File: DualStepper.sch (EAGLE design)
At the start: 12 parts

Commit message: Changed wire connectors to 5 mm grid
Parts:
- X1, X2: device con-phoenix-254:MPT4 -> con-ptr500:AK500/4
- X3: device con-phoenix-254:MPT2 -> con-ptr500:AK500/2
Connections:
- net +24V: now also X3-1.KL; no longer X3-2.1
- net GND: now also X3-2.KL; no longer X3-1.1
- net N$1: now also X1-1.KL; no longer X1-4.1
- net N$2: now also X1-2.KL; no longer X1-3.1
- net N$3: now also X1-3.KL; no longer X1-2.1
- net N$4: now also X1-4.KL; no longer X1-1.1
- net N$5: now also X2-4.KL; no longer X2-1.1
- net N$6: now also X2-3.KL; no longer X2-2.1
- net N$7: now also X2-2.KL; no longer X2-3.1
- net N$8: now also X2-1.KL; no longer X2-4.1
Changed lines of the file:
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@@
 <classes>
 <class number="0" name="default" width="0" drill="0">
-<clearance class="0" value="0.205"/>
 </class>
 </classes>
@@
 <part name="B1" library="we-board" deviceset="STEPSTICK" device="-TP"/>
 <part name="B2" library="we-board" deviceset="STEPSTICK" device="-TP"/>
-<part name="X1" library="con-phoenix-254" deviceset="MPT4" device=""/>
 <part name="GND1" library="supply1" deviceset="GND" device=""/>
 <part name="GND2" library="supply1" deviceset="GND" device=""/>
@@
 </part>
 <part name="GND4" library="supply1" deviceset="GND" device=""/>
-<part name="X3" library="con-phoenix-254" deviceset="MPT2" device=""/>
 <part name="GND5" library="supply1" deviceset="GND" device=""/>
 <part name="P+7" library="supply1" deviceset="+5V" device=""/>
@@
 <part name="GND7" library="supply1" deviceset="GND" device=""/>
 <part name="GND8" library="supply1" deviceset="GND" device=""/>
-<part name="X2" library="con-phoenix-254" deviceset="MPT4" device=""/>
+<part name="X1" library="con-ptr500" deviceset="AK500/4" device=""/>
+<part name="X2" library="con-ptr500" deviceset="AK500/4" device=""/>
+<part name="X3" library="con-ptr500" deviceset="AK500/2" device=""/>
 </parts>
 <sheets>
@@
 <instance part="B1" gate="BOARD" x="68.58" y="58.42"/>
 <instance part="B2" gate="BOARD" x="68.58" y="12.7"/>
-<instance part="X1" gate="-1" x="114.3" y="73.66"/>
-<instance part="X1" gate="-2" x="114.3" y="68.58"/>
-<instance part="X1" gate="-3" x="114.3" y="63.5"/>
-<instance part="X1" gate="-4" x="114.3" y="58.42"/>
 <instance part="GND1" gate="1" x="83.82" y="40.64"/>
 <instance part="GND2" gate="1" x="83.82" y="-7.62"/>
@@
 </instance>
 <instance part="GND4" gate="1" x="2.54" y="38.1"/>
-<instance part="X3" gate="-1" x="-15.24" y="71.12" rot="R180"/>
-<instance part="X3" gate="-2" x="-15.24" y="76.2" rot="R180"/>
 <instance part="GND5" gate="1" x="-7.62" y="71.12" rot="R90"/>
 <instance part="P+7" gate="1" x="17.78" y="30.48" rot="R180"/>
@@
 <instance part="GND7" gate="1" x="50.8" y="73.66" rot="R270"/>
 <instance part="GND8" gate="1" x="50.8" y="27.94" rot="R270"/>
-<instance part="X2" gate="-1" x="114.3" y="27.94"/>
-<instance part="X2" gate="-2" x="114.3" y="22.86"/>
-<instance part="X2" gate="-3" x="114.3" y="17.78"/>
-<instance part="X2" gate="-4" x="114.3" y="12.7"/>
+<instance part="X1" gate="-1" x="116.84" y="58.42" rot="R180"/>
+<instance part="X1" gate="-2" x="116.84" y="63.5" rot="R180"/>
+<instance part="X1" gate="-3" x="116.84" y="68.58" rot="R180"/>
+<instance part="X1" gate="-4" x="116.84" y="73.66" rot="R180"/>
+<instance part="X2" gate="-1" x="116.84" y="12.7" rot="R180"/>
+<instance part="X2" gate="-2" x="116.84" y="17.78" rot="R180"/>
+<instance part="X2" gate="-3" x="116.84" y="22.86" rot="R180"/>
+<instance part="X2" gate="-4" x="116.84" y="27.94" rot="R180"/>
+<instance part="X3" gate="-1" x="-17.78" y="76.2"/>
+<instance part="X3" gate="-2" x="-17.78" y="71.12"/>
 </instances>
 <busses>
@@
 </segment>
 <segment>
-<pinref part="X3" gate="-1" pin="1"/>
 <pinref part="GND5" gate="1" pin="GND"/>
 <wire x1="-12.7" y1="71.12" x2="-10.16" y2="71.12" width="0.1524" layer="91"/>
+<pinref part="X3" gate="-2" pin="KL"/>
 </segment>
 <segment>
@@
 <net name="+24V" class="0">
 <segment>
-<pinref part="X3" gate="-2" pin="1"/>
 <pinref part="P+6" gate="1" pin="+24V"/>
 <wire x1="-12.7" y1="76.2" x2="-10.16" y2="76.2" width="0.1524" layer="91"/>
+<pinref part="X3" gate="-1" pin="KL"/>
 </segment>
 <segment>
@@
 <net name="N$1" class="0">
 <segment>
-<pinref part="X1" gate="-4" pin="1"/>
 <pinref part="B1" gate="BOARD" pin="M2B"/>
 <wire x1="111.76" y1="58.42" x2="81.28" y2="58.42" width="0.1524" layer="91"/>
+<pinref part="X1" gate="-1" pin="KL"/>
 </segment>
 </net>
 <net name="N$2" class="0">
 <segment>
-<pinref part="X1" gate="-3" pin="1"/>
 <pinref part="B1" gate="BOARD" pin="M2A"/>
 <wire x1="111.76" y1="63.5" x2="81.28" y2="63.5" width="0.1524" layer="91"/>
+<pinref part="X1" gate="-2" pin="KL"/>
 </segment>
 </net>
 <net name="N$3" class="0">
 <segment>
-<pinref part="X1" gate="-2" pin="1"/>
 <pinref part="B1" gate="BOARD" pin="M1A"/>
 <wire x1="111.76" y1="68.58" x2="81.28" y2="68.58" width="0.1524" layer="91"/>
+<pinref part="X1" gate="-3" pin="KL"/>
 </segment>
 </net>
 <net name="N$4" class="0">
 <segment>
-<pinref part="X1" gate="-1" pin="1"/>
 <pinref part="B1" gate="BOARD" pin="M1B"/>
 <wire x1="111.76" y1="73.66" x2="81.28" y2="73.66" width="0.1524" layer="91"/>
+<pinref part="X1" gate="-4" pin="KL"/>
 </segment>
 </net>
@@
 <segment>
 <pinref part="B2" gate="BOARD" pin="M1B"/>
-<pinref part="X2" gate="-1" pin="1"/>
 <wire x1="81.28" y1="27.94" x2="111.76" y2="27.94" width="0.1524" layer="91"/>
+<pinref part="X2" gate="-4" pin="KL"/>
 </segment>
 </net>
@@
 <segment>
 <pinref part="B2" gate="BOARD" pin="M1A"/>
-<pinref part="X2" gate="-2" pin="1"/>
 <wire x1="81.28" y1="22.86" x2="111.76" y2="22.86" width="0.1524" layer="91"/>
+<pinref part="X2" gate="-3" pin="KL"/>
 </segment>
 </net>
@@
 <segment>
 <pinref part="B2" gate="BOARD" pin="M2A"/>
-<pinref part="X2" gate="-3" pin="1"/>
 <wire x1="81.28" y1="17.78" x2="111.76" y2="17.78" width="0.1524" layer="91"/>
+<pinref part="X2" gate="-2" pin="KL"/>
 </segment>
 </net>
@@
 <segment>
 <pinref part="B2" gate="BOARD" pin="M2B"/>
-<pinref part="X2" gate="-4" pin="1"/>
 <wire x1="81.28" y1="12.7" x2="111.76" y2="12.7" width="0.1524" layer="91"/>
-</segment>
-</net>
+<pinref part="X2" gate="-1" pin="KL"/>
+</segment>
+</net>

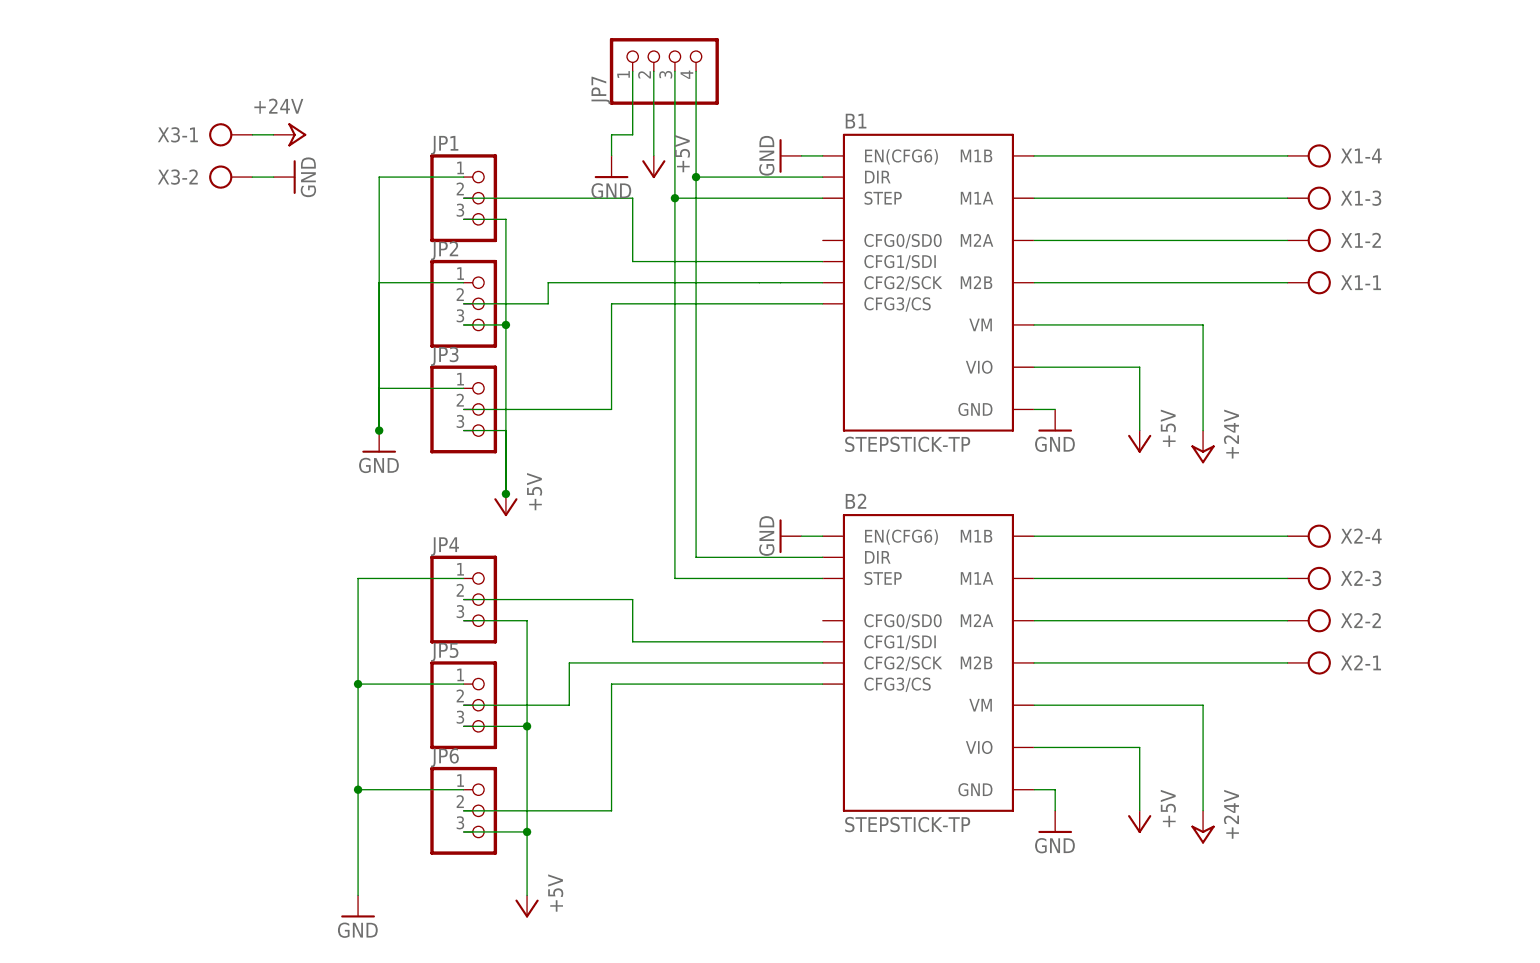
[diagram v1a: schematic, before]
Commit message: Changed connectors to 3.5 RT
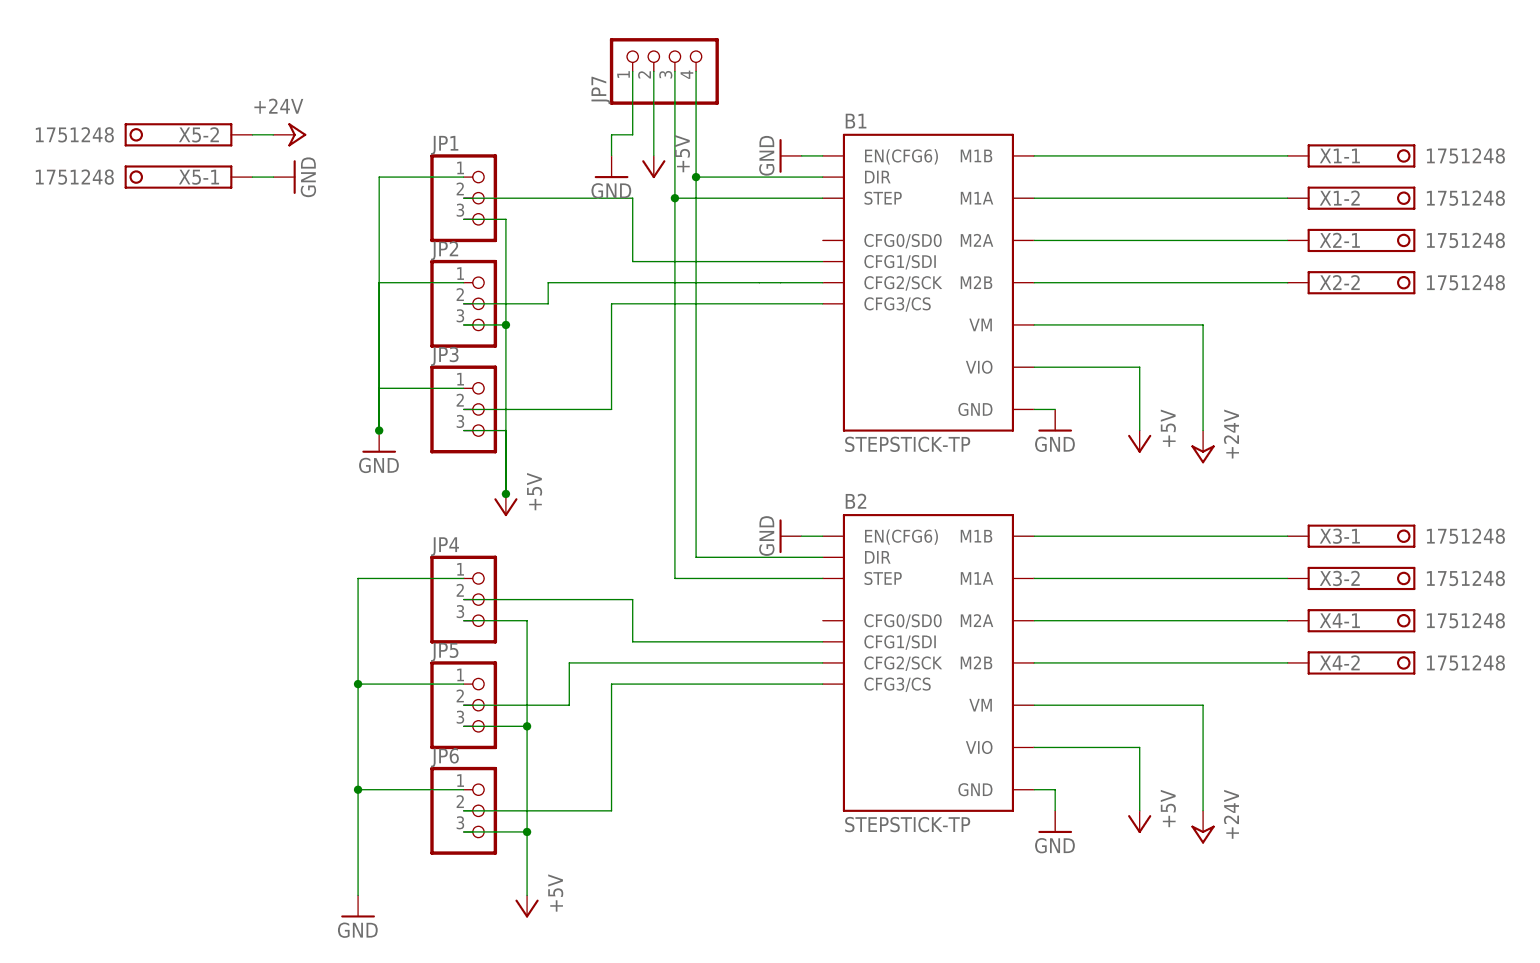
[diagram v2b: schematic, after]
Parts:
- added X4, X5: 1751248, con-phoenix-350:1751248
- X1, X2: value (none) -> 1751248; device con-ptr500:AK500/4 -> con-phoenix-350:1751248
- X3: value (none) -> 1751248; device con-ptr500:AK500/2 -> con-phoenix-350:1751248
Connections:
- net +24V: now also X5-2.K; no longer X3-1.KL
- net GND: now also X5-1.K; no longer X3-2.KL
- net N$1: now also X2-2.K; no longer X1-1.KL
- net N$2: now also X2-1.K; no longer X1-2.KL
- net N$3: now also X1-2.K; no longer X1-3.KL
- net N$4: now also X1-1.K; no longer X1-4.KL
- net N$5: now also X3-1.K; no longer X2-4.KL
- net N$6: now also X3-2.K; no longer X2-3.KL
- net N$7: now also X4-1.K; no longer X2-2.KL
- net N$8: now also X4-2.K; no longer X2-1.KL
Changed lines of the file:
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@@
 <grid distance="0.1" unitdist="inch" unit="inch" style="lines" multiple="1" display="no" altdistance="0.01" altunitdist="inch" altunit="inch"/>
 <layers>
-<layer number="1" name="Top" color="4" fill="1" visible="no" active="no"/>
-<layer number="16" name="Bottom" color="1" fill="1" visible="no" active="no"/>
-<layer number="17" name="Pads" color="2" fill="1" visible="no" active="no"/>
-<layer number="18" name="Vias" color="2" fill="1" visible="no" active="no"/>
-<layer number="19" name="Unrouted" color="6" fill="1" visible="no" active="no"/>
-<layer number="20" name="Dimension" color="15" fill="1" visible="no" active="no"/>
-<layer number="21" name="tPlace" color="7" fill="1" visible="no" active="no"/>
-<layer number="22" name="bPlace" color="7" fill="1" visible="no" active="no"/>
-<layer number="23" name="tOrigins" color="15" fill="1" visible="no" active="no"/>
-<layer number="24" name="bOrigins" color="15" fill="1" visible="no" active="no"/>
-<layer number="25" name="tNames" color="7" fill="1" visible="no" active="no"/>
-<layer number="26" name="bNames" color="7" fill="1" visible="no" active="no"/>
-<layer number="27" name="tValues" color="7" fill="1" visible="no" active="no"/>
-<layer number="28" name="bValues" color="7" fill="1" visible="no" active="no"/>
+<layer number="1" name="Top" color="4" fill="1" visible="yes" active="no"/>
+<layer number="16" name="Bottom" color="1" fill="1" visible="yes" active="no"/>
+<layer number="17" name="Pads" color="2" fill="1" visible="yes" active="no"/>
+<layer number="18" name="Vias" color="2" fill="1" visible="yes" active="no"/>
+<layer number="19" name="Unrouted" color="6" fill="1" visible="yes" active="no"/>
+<layer number="20" name="Dimension" color="15" fill="1" visible="yes" active="no"/>
+<layer number="21" name="tPlace" color="7" fill="1" visible="yes" active="no"/>
+<layer number="22" name="bPlace" color="7" fill="1" visible="yes" active="no"/>
+<layer number="23" name="tOrigins" color="15" fill="1" visible="yes" active="no"/>
+<layer number="24" name="bOrigins" color="15" fill="1" visible="yes" active="no"/>
+<layer number="25" name="tNames" color="7" fill="1" visible="yes" active="no"/>
+<layer number="26" name="bNames" color="7" fill="1" visible="yes" active="no"/>
+<layer number="27" name="tValues" color="7" fill="1" visible="yes" active="no"/>
+<layer number="28" name="bValues" color="7" fill="1" visible="yes" active="no"/>
 <layer number="29" name="tStop" color="7" fill="3" visible="no" active="no"/>
 <layer number="30" name="bStop" color="7" fill="6" visible="no" active="no"/>
@@
 <layer number="35" name="tGlue" color="7" fill="4" visible="no" active="no"/>
 <layer number="36" name="bGlue" color="7" fill="5" visible="no" active="no"/>
-<layer number="37" name="tTest" color="7" fill="1" visible="no" active="no"/>
-<layer number="38" name="bTest" color="7" fill="1" visible="no" active="no"/>
+<layer number="37" name="tTest" color="7" fill="1" visible="yes" active="no"/>
+<layer number="38" name="bTest" color="7" fill="1" visible="yes" active="no"/>
 <layer number="39" name="tKeepout" color="4" fill="11" visible="no" active="no"/>
 <layer number="40" name="bKeepout" color="1" fill="11" visible="no" active="no"/>
@@
 <layer number="44" name="Drills" color="7" fill="1" visible="no" active="no"/>
 <layer number="45" name="Holes" color="7" fill="1" visible="no" active="no"/>
-<layer number="46" name="Milling" color="3" fill="1" visible="no" active="no"/>
-<layer number="47" name="Measures" color="7" fill="1" visible="no" active="no"/>
-<layer number="48" name="Document" color="7" fill="1" visible="no" active="no"/>
-<layer number="49" name="Reference" color="7" fill="1" visible="no" active="no"/>
-<layer number="51" name="tDocu" color="7" fill="1" visible="no" active="no"/>
-<layer number="52" name="bDocu" color="7" fill="1" visible="no" active="no"/>
+<layer number="46" name="Milling" color="3" fill="1" visible="yes" active="no"/>
+<layer number="47" name="Measures" color="7" fill="1" visible="yes" active="no"/>
+<layer number="48" name="Document" color="7" fill="1" visible="yes" active="no"/>
+<layer number="49" name="Reference" color="7" fill="1" visible="yes" active="no"/>
+<layer number="51" name="tDocu" color="7" fill="1" visible="yes" active="no"/>
+<layer number="52" name="bDocu" color="7" fill="1" visible="yes" active="no"/>
 <layer number="90" name="Modules" color="5" fill="1" visible="yes" active="yes"/>
 <layer number="91" name="Nets" color="2" fill="1" visible="yes" active="yes"/>
@@
 <part name="GND7" library="supply1" deviceset="GND" device=""/>
 <part name="GND8" library="supply1" deviceset="GND" device=""/>
-<part name="X1" library="con-ptr500" deviceset="AK500/4" device=""/>
-<part name="X2" library="con-ptr500" deviceset="AK500/4" device=""/>
-<part name="X3" library="con-ptr500" deviceset="AK500/2" device=""/>
+<part name="X1" library="con-phoenix-350" deviceset="1751248" device=""/>
+<part name="X2" library="con-phoenix-350" deviceset="1751248" device=""/>
+<part name="X3" library="con-phoenix-350" deviceset="1751248" device=""/>
+<part name="X4" library="con-phoenix-350" deviceset="1751248" device=""/>
+<part name="X5" library="con-phoenix-350" deviceset="1751248" device=""/>
 </parts>
 <sheets>
@@
 <instance part="GND7" gate="1" x="50.8" y="73.66" rot="R270"/>
 <instance part="GND8" gate="1" x="50.8" y="27.94" rot="R270"/>
-<instance part="X1" gate="-1" x="116.84" y="58.42" rot="R180"/>
-<instance part="X1" gate="-2" x="116.84" y="63.5" rot="R180"/>
-<instance part="X1" gate="-3" x="116.84" y="68.58" rot="R180"/>
-<instance part="X1" gate="-4" x="116.84" y="73.66" rot="R180"/>
-<instance part="X2" gate="-1" x="116.84" y="12.7" rot="R180"/>
-<instance part="X2" gate="-2" x="116.84" y="17.78" rot="R180"/>
-<instance part="X2" gate="-3" x="116.84" y="22.86" rot="R180"/>
-<instance part="X2" gate="-4" x="116.84" y="27.94" rot="R180"/>
-<instance part="X3" gate="-1" x="-17.78" y="76.2"/>
-<instance part="X3" gate="-2" x="-17.78" y="71.12"/>
+<instance part="X1" gate="-1" x="114.3" y="73.66"/>
+<instance part="X1" gate="-2" x="114.3" y="68.58"/>
+<instance part="X2" gate="-1" x="114.3" y="63.5"/>
+<instance part="X2" gate="-2" x="114.3" y="58.42"/>
+<instance part="X3" gate="-1" x="114.3" y="27.94"/>
+<instance part="X3" gate="-2" x="114.3" y="22.86"/>
+<instance part="X4" gate="-1" x="114.3" y="17.78"/>
+<instance part="X4" gate="-2" x="114.3" y="12.7"/>
+<instance part="X5" gate="-1" x="-15.24" y="71.12" rot="R180"/>
+<instance part="X5" gate="-2" x="-15.24" y="76.2" rot="R180"/>
 </instances>
 <busses>
@@
 <pinref part="GND5" gate="1" pin="GND"/>
 <wire x1="-12.7" y1="71.12" x2="-10.16" y2="71.12" width="0.1524" layer="91"/>
-<pinref part="X3" gate="-2" pin="KL"/>
+<pinref part="X5" gate="-1" pin="K"/>
 </segment>
 <segment>
@@
 <pinref part="P+6" gate="1" pin="+24V"/>
 <wire x1="-12.7" y1="76.2" x2="-10.16" y2="76.2" width="0.1524" layer="91"/>
-<pinref part="X3" gate="-1" pin="KL"/>
+<pinref part="X5" gate="-2" pin="K"/>
 </segment>
 <segment>
@@
 <pinref part="B1" gate="BOARD" pin="M2B"/>
 <wire x1="111.76" y1="58.42" x2="81.28" y2="58.42" width="0.1524" layer="91"/>
-<pinref part="X1" gate="-1" pin="KL"/>
+<pinref part="X2" gate="-2" pin="K"/>
 </segment>
 </net>
@@
 <pinref part="B1" gate="BOARD" pin="M2A"/>
 <wire x1="111.76" y1="63.5" x2="81.28" y2="63.5" width="0.1524" layer="91"/>
-<pinref part="X1" gate="-2" pin="KL"/>
+<pinref part="X2" gate="-1" pin="K"/>
 </segment>
 </net>
@@
 <pinref part="B1" gate="BOARD" pin="M1A"/>
 <wire x1="111.76" y1="68.58" x2="81.28" y2="68.58" width="0.1524" layer="91"/>
-<pinref part="X1" gate="-3" pin="KL"/>
+<pinref part="X1" gate="-2" pin="K"/>
 </segment>
 </net>
@@
 <pinref part="B1" gate="BOARD" pin="M1B"/>
 <wire x1="111.76" y1="73.66" x2="81.28" y2="73.66" width="0.1524" layer="91"/>
-<pinref part="X1" gate="-4" pin="KL"/>
+<pinref part="X1" gate="-1" pin="K"/>
 </segment>
 </net>
@@
 <pinref part="B2" gate="BOARD" pin="M1B"/>
 <wire x1="81.28" y1="27.94" x2="111.76" y2="27.94" width="0.1524" layer="91"/>
-<pinref part="X2" gate="-4" pin="KL"/>
+<pinref part="X3" gate="-1" pin="K"/>
 </segment>
 </net>
@@
 <pinref part="B2" gate="BOARD" pin="M1A"/>
 <wire x1="81.28" y1="22.86" x2="111.76" y2="22.86" width="0.1524" layer="91"/>
-<pinref part="X2" gate="-3" pin="KL"/>
+<pinref part="X3" gate="-2" pin="K"/>
 </segment>
 </net>
@@
 <pinref part="B2" gate="BOARD" pin="M2A"/>
 <wire x1="81.28" y1="17.78" x2="111.76" y2="17.78" width="0.1524" layer="91"/>
-<pinref part="X2" gate="-2" pin="KL"/>
+<pinref part="X4" gate="-1" pin="K"/>
 </segment>
 </net>
@@
 <pinref part="B2" gate="BOARD" pin="M2B"/>
 <wire x1="81.28" y1="12.7" x2="111.76" y2="12.7" width="0.1524" layer="91"/>
-<pinref part="X2" gate="-1" pin="KL"/>
-</segment>
-</net>
+<pinref part="X4" gate="-2" pin="K"/>
+</segment>
+</net>

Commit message: Added PartNaming
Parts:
- renumbered B1 to STEPDRV1, B2 to STEPDRV2, JP1 to S1CFG1, JP2 to S1CFG2, JP3 to S1CFG3, JP4 to S2CFG1, JP5 to S2CFG2, JP6 to S2CFG3, X1 to ST1M1, X2 to ST1M2, X3 to ST2M1, X4 to ST2M2, X5 to VM
